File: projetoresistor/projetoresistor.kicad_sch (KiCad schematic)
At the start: 1 part

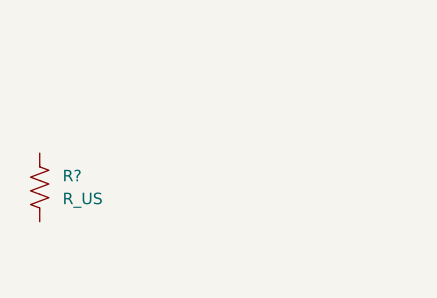
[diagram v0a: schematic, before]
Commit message: dois resistores e coaxial
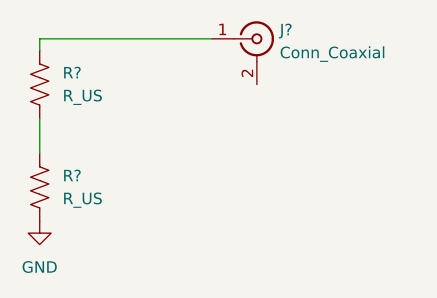
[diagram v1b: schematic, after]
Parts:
- added J?: Conn_Coaxial, symbol Connector:Conn_Coaxial
- added R?: R_US, symbol Device:R_US
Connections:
- net at R?.1: now also R?.2
- net GND: now reaches R?.2
- new net: J?.1 (In), R?.1
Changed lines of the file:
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@@
 (kicad_sch (version 20211123) (generator eeschema)
   (paper "A4")
+  (wire (pts (xy 121.92 82.55) (xy 121.92 86.36))
+    (stroke (width 0) (type default) (color 0 0 0 0))
+  )
+  (wire (pts (xy 121.92 73.66) (xy 121.92 74.93))
+    (stroke (width 0) (type default) (color 0 0 0 0))
+  )
+  (wire (pts (xy 140.97 73.66) (xy 121.92 73.66))
+    (stroke (width 0) (type default) (color 0 0 0 0))
+  )
+  (symbol (lib_id "power:GND") (at 121.92 93.98 0) (unit 1)
+    (in_bom yes) (on_board yes) (fields_autoplaced)
+    (property "Reference" "#PWR?" (id 0) (at 121.92 100.33 0)
+      (effects (font (size 1.27 1.27)) hide)
+    )
+    (property "Value" "GND" (id 1) (at 121.92 99.06 0))
+    (property "Footprint" "" (id 2) (at 121.92 93.98 0)
+      (effects (font (size 1.27 1.27)) hide)
+    )
+    (property "Datasheet" "" (id 3) (at 121.92 93.98 0)
+      (effects (font (size 1.27 1.27)) hide)
+    )
+    (pin "1")
+  )
   (symbol (lib_id "Device:R_US") (at 121.92 90.17 0) (unit 1)
     (in_bom yes) (on_board yes) (fields_autoplaced)
@@
     (pin "2")
   )
+  (symbol (lib_id "Device:R_US") (at 121.92 78.74 0) (unit 1)
+    (in_bom yes) (on_board yes) (fields_autoplaced)
+    (property "Reference" "R?" (id 0) (at 124.46 77.4699 0)
+      (effects (font (size 1.27 1.27)) (justify left))
+    )
+    (property "Value" "R_US" (id 1) (at 124.46 80.0099 0)
+      (effects (font (size 1.27 1.27)) (justify left))
+    )
+    (property "Footprint" "" (id 2) (at 122.936 78.994 90)
+      (effects (font (size 1.27 1.27)) hide)
+    )
+    (property "Datasheet" "~" (id 3) (at 121.92 78.74 0)
+      (effects (font (size 1.27 1.27)) hide)
+    )
+    (pin "1")
+    (pin "2")
+  )
+  (symbol (lib_id "Connector:Conn_Coaxial") (at 146.05 73.66 0) (unit 1)
+    (in_bom yes) (on_board yes) (fields_autoplaced)
+    (property "Reference" "J?" (id 0) (at 148.59 72.6831 0)
+      (effects (font (size 1.27 1.27)) (justify left))
+    )
+    (property "Value" "Conn_Coaxial" (id 1) (at 148.59 75.2231 0)
+      (effects (font (size 1.27 1.27)) (justify left))
+    )
+    (property "Footprint" "" (id 2) (at 146.05 73.66 0)
+      (effects (font (size 1.27 1.27)) hide)
+    )
+    (property "Datasheet" " ~" (id 3) (at 146.05 73.66 0)
+      (effects (font (size 1.27 1.27)) hide)
+    )
+    (pin "1")
+    (pin "2")
+  )
   (sheet_instances
     (path "/" (page "1"))
   )
   (symbol_instances
+    (path "/2c9af68b-ecd0-4f17-a58c-04914790416c"
+      (reference "#PWR?") (unit 1) (value "GND") (footprint "")
+    )
+    (path "/9cb98fbc-e0bc-43ae-86fb-8d3592b3449d"
+      (reference "J?") (unit 1) (value "Conn_Coaxial") (footprint "")
+    )
     (path "/8f60cf54-c303-437b-8aec-67fbe4fb1281"
       (reference "R?") (unit 1) (value "R_US") (footprint "")
     )
+    (path "/94cdf711-e6b6-4a2a-87e5-3a7d5ec80fb0"
+      (reference "R?") (unit 1) (value "R_US") (footprint "")
+    )

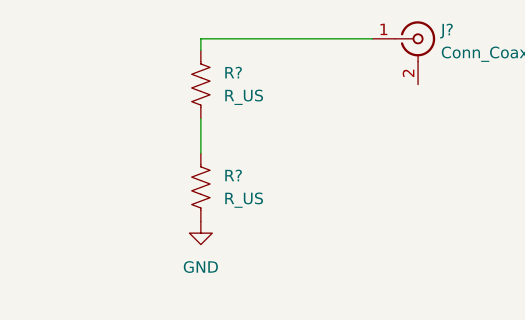
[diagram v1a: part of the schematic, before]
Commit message: adicionando capacitor
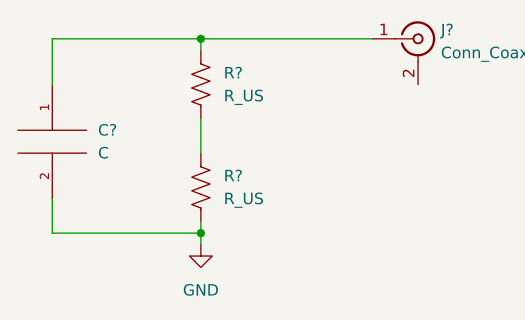
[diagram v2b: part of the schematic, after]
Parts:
- added C?: C, symbol pspice:C
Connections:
- net GND: now also C?.2
- net at J?.1 (In), R?.1: now also C?.1
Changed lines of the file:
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@@
 (kicad_sch (version 20211123) (generator eeschema)
   (paper "A4")
+  (junction (at 121.92 73.66) (diameter 0) (color 0 0 0 0)
+  )
+  (junction (at 121.92 95.25) (diameter 0) (color 0 0 0 0)
+  )
+  (wire (pts (xy 105.41 78.74) (xy 105.41 73.66))
+    (stroke (width 0) (type default) (color 0 0 0 0))
+  )
+  (wire (pts (xy 121.92 96.52) (xy 121.92 95.25))
+    (stroke (width 0) (type default) (color 0 0 0 0))
+  )
   (wire (pts (xy 121.92 82.55) (xy 121.92 86.36))
+    (stroke (width 0) (type default) (color 0 0 0 0))
+  )
+  (wire (pts (xy 105.41 91.44) (xy 105.41 95.25))
+    (stroke (width 0) (type default) (color 0 0 0 0))
+  )
+  (wire (pts (xy 105.41 95.25) (xy 121.92 95.25))
+    (stroke (width 0) (type default) (color 0 0 0 0))
+  )
+  (wire (pts (xy 105.41 73.66) (xy 121.92 73.66))
+    (stroke (width 0) (type default) (color 0 0 0 0))
+  )
+  (wire (pts (xy 121.92 95.25) (xy 121.92 93.98))
     (stroke (width 0) (type default) (color 0 0 0 0))
   )
@@
     (stroke (width 0) (type default) (color 0 0 0 0))
   )
-  (symbol (lib_id "power:GND") (at 121.92 93.98 0) (unit 1)
+  (symbol (lib_id "power:GND") (at 121.92 96.52 0) (unit 1)
     (in_bom yes) (on_board yes) (fields_autoplaced)
-    (property "Reference" "#PWR?" (id 0) (at 121.92 100.33 0)
+    (property "Reference" "#PWR?" (id 0) (at 121.92 102.87 0)
       (effects (font (size 1.27 1.27)) hide)
     )
-    (property "Value" "GND" (id 1) (at 121.92 99.06 0))
-    (property "Footprint" "" (id 2) (at 121.92 93.98 0)
+    (property "Value" "GND" (id 1) (at 121.92 101.6 0))
+    (property "Footprint" "" (id 2) (at 121.92 96.52 0)
       (effects (font (size 1.27 1.27)) hide)
     )
-    (property "Datasheet" "" (id 3) (at 121.92 93.98 0)
+    (property "Datasheet" "" (id 3) (at 121.92 96.52 0)
       (effects (font (size 1.27 1.27)) hide)
     )
@@
     (pin "2")
   )
+  (symbol (lib_id "pspice:C") (at 105.41 85.09 0) (unit 1)
+    (in_bom yes) (on_board yes) (fields_autoplaced)
+    (property "Reference" "C?" (id 0) (at 110.49 83.8199 0)
+      (effects (font (size 1.27 1.27)) (justify left))
+    )
+    (property "Value" "C" (id 1) (at 110.49 86.3599 0)
+      (effects (font (size 1.27 1.27)) (justify left))
+    )
+    (property "Footprint" "" (id 2) (at 105.41 85.09 0)
+      (effects (font (size 1.27 1.27)) hide)
+    )
+    (property "Datasheet" "~" (id 3) (at 105.41 85.09 0)
+      (effects (font (size 1.27 1.27)) hide)
+    )
+    (pin "1")
+    (pin "2")
+  )
   (sheet_instances
     (path "/" (page "1"))
@@
       (reference "#PWR?") (unit 1) (value "GND") (footprint "")
     )
+    (path "/a21c2d5b-b67f-45ee-b988-c235636c4748"
+      (reference "C?") (unit 1) (value "C") (footprint "")
+    )
     (path "/9cb98fbc-e0bc-43ae-86fb-8d3592b3449d"

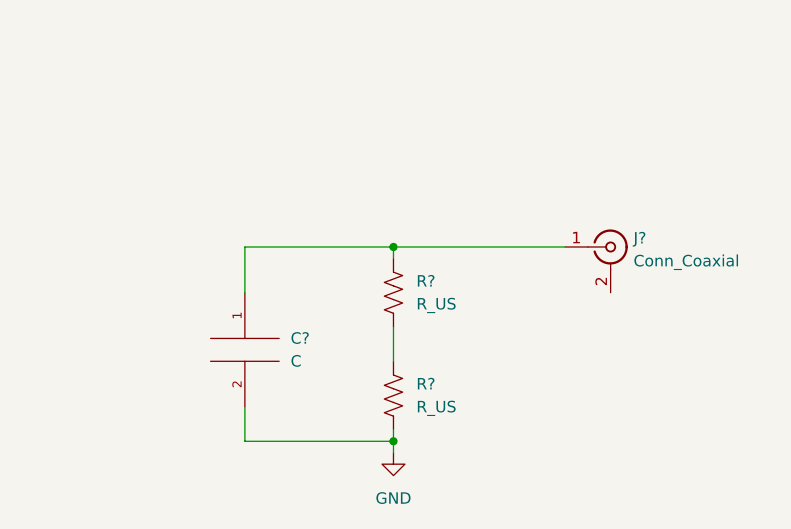
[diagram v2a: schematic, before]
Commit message: completando circuito final com cap
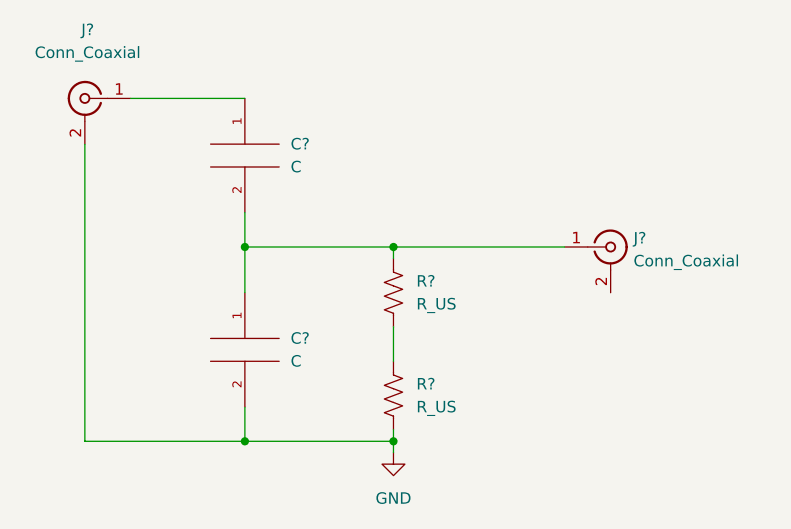
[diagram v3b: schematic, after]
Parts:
- added C?: C, symbol pspice:C
- added J?: Conn_Coaxial, symbol Connector:Conn_Coaxial
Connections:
- net GND: now also J?.2 (Ext)
- net at C?.1, J?.1 (In), R?.1: now also C?.2
- new net: C?.1, J?.1 (In)
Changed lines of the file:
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@@
 (kicad_sch (version 20211123) (generator eeschema)
   (paper "A4")
+  (junction (at 105.41 73.66) (diameter 0) (color 0 0 0 0)
+  )
+  (junction (at 105.41 95.25) (diameter 0) (color 0 0 0 0)
+  )
   (junction (at 121.92 73.66) (diameter 0) (color 0 0 0 0)
   )
   (junction (at 121.92 95.25) (diameter 0) (color 0 0 0 0)
+  )
+  (wire (pts (xy 92.71 57.15) (xy 105.41 57.15))
+    (stroke (width 0) (type default) (color 0 0 0 0))
   )
   (wire (pts (xy 105.41 78.74) (xy 105.41 73.66))
@@
   )
   (wire (pts (xy 121.92 96.52) (xy 121.92 95.25))
+    (stroke (width 0) (type default) (color 0 0 0 0))
+  )
+  (wire (pts (xy 87.63 62.23) (xy 87.63 95.25))
     (stroke (width 0) (type default) (color 0 0 0 0))
   )
@@
     (stroke (width 0) (type default) (color 0 0 0 0))
   )
+  (wire (pts (xy 87.63 95.25) (xy 105.41 95.25))
+    (stroke (width 0) (type default) (color 0 0 0 0))
+  )
   (wire (pts (xy 105.41 95.25) (xy 121.92 95.25))
     (stroke (width 0) (type default) (color 0 0 0 0))
   )
   (wire (pts (xy 105.41 73.66) (xy 121.92 73.66))
+    (stroke (width 0) (type default) (color 0 0 0 0))
+  )
+  (wire (pts (xy 105.41 69.85) (xy 105.41 73.66))
     (stroke (width 0) (type default) (color 0 0 0 0))
   )
@@
     )
     (pin "1")
+  )
+  (symbol (lib_id "Connector:Conn_Coaxial") (at 87.63 57.15 0) (mirror y) (unit 1)
+    (in_bom yes) (on_board yes) (fields_autoplaced)
+    (property "Reference" "J?" (id 0) (at 87.9474 49.53 0))
+    (property "Value" "Conn_Coaxial" (id 1) (at 87.9474 52.07 0))
+    (property "Footprint" "" (id 2) (at 87.63 57.15 0)
+      (effects (font (size 1.27 1.27)) hide)
+    )
+    (property "Datasheet" " ~" (id 3) (at 87.63 57.15 0)
+      (effects (font (size 1.27 1.27)) hide)
+    )
+    (pin "1")
+    (pin "2")
   )
   (symbol (lib_id "Device:R_US") (at 121.92 90.17 0) (unit 1)
@@
     (pin "2")
   )
+  (symbol (lib_id "pspice:C") (at 105.41 63.5 0) (unit 1)
+    (in_bom yes) (on_board yes) (fields_autoplaced)
+    (property "Reference" "C?" (id 0) (at 110.49 62.2299 0)
+      (effects (font (size 1.27 1.27)) (justify left))
+    )
+    (property "Value" "C" (id 1) (at 110.49 64.7699 0)
+      (effects (font (size 1.27 1.27)) (justify left))
+    )
+    (property "Footprint" "" (id 2) (at 105.41 63.5 0)
+      (effects (font (size 1.27 1.27)) hide)
+    )
+    (property "Datasheet" "~" (id 3) (at 105.41 63.5 0)
+      (effects (font (size 1.27 1.27)) hide)
+    )
+    (pin "1")
+    (pin "2")
+  )
   (sheet_instances
     (path "/" (page "1"))
@@
       (reference "C?") (unit 1) (value "C") (footprint "")
     )
+    (path "/e9aac3c0-c7cf-4d95-8e9a-4ea9936a98cc"
+      (reference "C?") (unit 1) (value "C") (footprint "")
+    )
+    (path "/5da32575-3636-4139-b2e5-417a0547d9a4"
+      (reference "J?") (unit 1) (value "Conn_Coaxial") (footprint "")
+    )
     (path "/9cb98fbc-e0bc-43ae-86fb-8d3592b3449d"
